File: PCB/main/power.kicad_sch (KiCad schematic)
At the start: 28 parts, among them M1 CJ2301 S1, U1 LP2951-33DR, U2 LM324

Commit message: circuit edits
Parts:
- removed D2: BAT54S, Diode_SMD:D_SOT-23_ANK, symbol Device:D_Schottky
- removed M1: CJ2301 S1, Package_TO_SOT_SMD:SOT-23, symbol pspice:MPMOS
- added D?: ZMM5V1-M, symbol Device:D_Zener
- added Q?: Q_PMOS_SGD, symbol Device:Q_PMOS_SGD
- added Q?: Q_PMOS_GSD, symbol Device:Q_PMOS_GSD
- added R?: 100, symbol Device:R
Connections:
- net +5V (INPUT PROTECTED): now also D?.1 (K), Q?.1 (S)
- net GND: now also R?.2
- net at D6.2 (A): now also Q?.2 (S)
- net at JP3.2 (B), JP4.2 (B): now also Q?.3 (D)
- net at JP6.2 (B), R3.1, U2.4 (V+): now also R5.2, Q?.3 (D); no longer R5.1
- net at D4.1 (K), U2.1 (+): now also R5.1; no longer R5.2
- net at U2.3: now also Q?.1 (G)
- new net: D?.2 (A), Q?.2 (G), R?.1
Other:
- moved on the sheet: D4, D6, JP3, JP4, JP6, R3, R4, R5, R6, U2

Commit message: Small changes
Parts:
- gave numbers to parts that had none: 4
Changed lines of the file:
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@@
   (symbol (lib_id "Device:Q_PMOS_SGD") (at 78.74 90.17 90) (unit 1)
     (in_bom yes) (on_board yes) (fields_autoplaced)
-    (property "Reference" "Q?" (id 0) (at 78.74 80.01 90))
+    (property "Reference" "Q2" (id 0) (at 78.74 80.01 90))
     (property "Value" "Q_PMOS_SGD" (id 1) (at 78.74 82.55 90))
     (property "Footprint" "" (id 2) (at 76.2 85.09 0)
@@
   (symbol (lib_id "Device:D_Zener") (at 88.9 91.44 270) (unit 1)
     (in_bom yes) (on_board yes) (fields_autoplaced)
-    (property "Reference" "D?" (id 0) (at 91.44 90.1699 90)
+    (property "Reference" "D2" (id 0) (at 91.44 90.1699 90)
       (effects (font (size 1.27 1.27)) (justify left))
     )
@@
   (symbol (lib_id "power:GND") (at 78.74 104.14 0) (unit 1)
     (in_bom yes) (on_board yes) (fields_autoplaced)
-    (property "Reference" "#PWR?" (id 0) (at 78.74 110.49 0)
+    (property "Reference" "#PWR019" (id 0) (at 78.74 110.49 0)
       (effects (font (size 1.27 1.27)) hide)
     )
@@
   (symbol (lib_id "Device:Q_PMOS_GSD") (at 255.27 50.8 0) (unit 1)
     (in_bom yes) (on_board yes) (fields_autoplaced)
-    (property "Reference" "Q?" (id 0) (at 261.62 49.5299 0)
+    (property "Reference" "Q3" (id 0) (at 261.62 49.5299 0)
       (effects (font (size 1.27 1.27)) (justify left))
     )
@@
   (symbol (lib_id "Device:R") (at 78.74 100.33 0) (unit 1)
     (in_bom yes) (on_board yes) (fields_autoplaced)
-    (property "Reference" "R?" (id 0) (at 81.28 99.0599 0)
-      (effects (font (size 1.27 1.27)) (justify left))
-    )
+    (property "Reference" "R19" (id 0) (at 81.28 99.0599 0)
+      (effects (font (size 1.27 1.27)) (justify left))
+    )

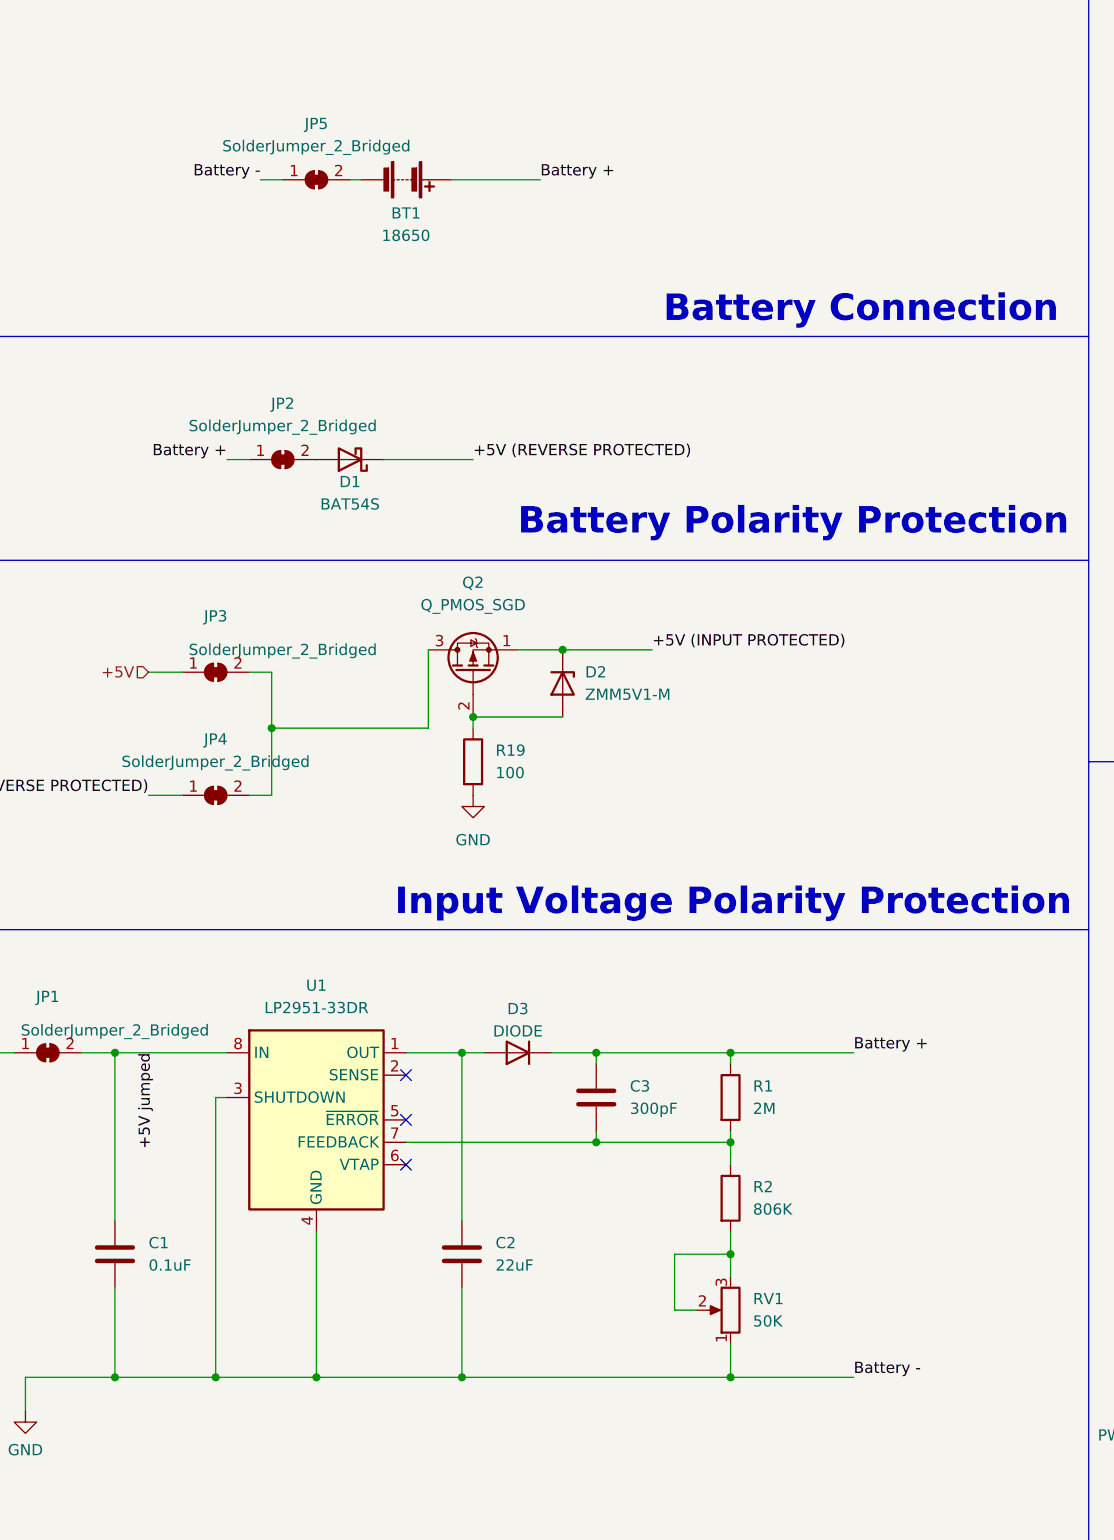
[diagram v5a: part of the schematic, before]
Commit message: Change labels
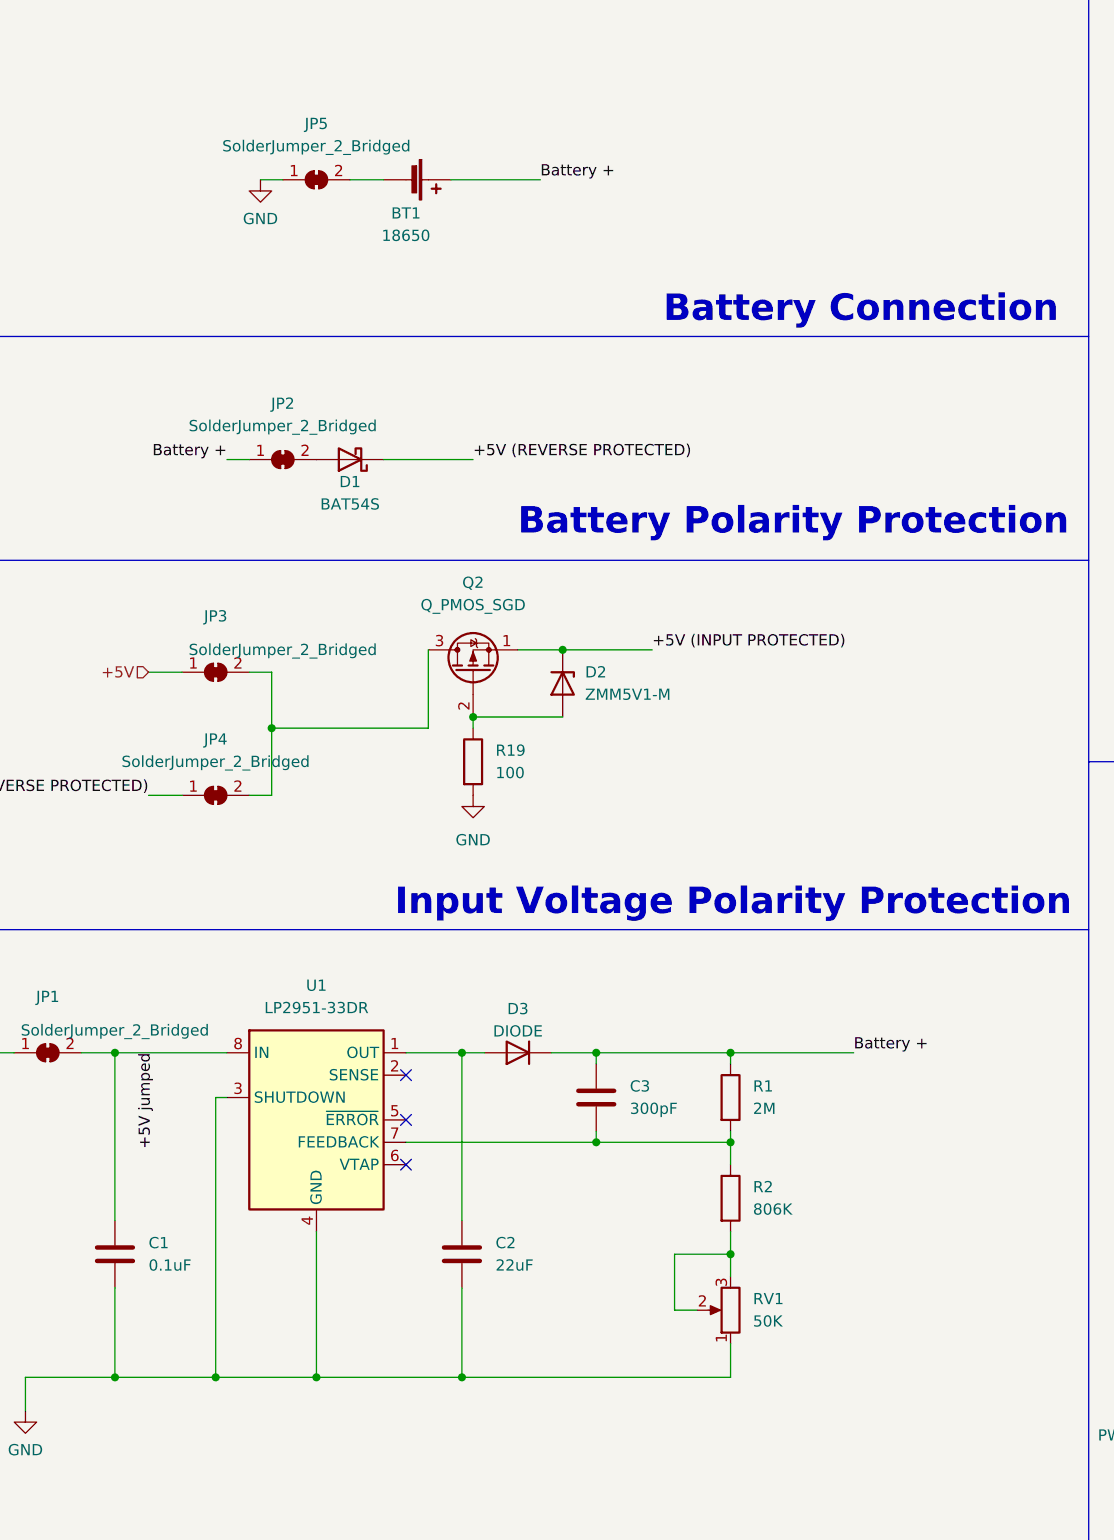
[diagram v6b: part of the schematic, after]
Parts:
- BT1: symbol Device:Battery -> Device:Battery_Cell
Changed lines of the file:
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@@
   (junction (at 78.74 95.25) (diameter 0) (color 0 0 0 0)
-  )
-  (junction (at 107.95 170.18) (diameter 0) (color 0 0 0 0)
   )
   (junction (at 55.88 96.52) (diameter 0) (color 0 0 0 0)
@@
     (stroke (width 0) (type default) (color 0 0 0 0))
   )
-  (wire (pts (xy 107.95 170.18) (xy 121.92 170.18))
-    (stroke (width 0) (type default) (color 0 0 0 0))
-  )
   (wire (pts (xy 71.12 133.35) (xy 77.47 133.35))
     (stroke (width 0) (type default) (color 0 0 0 0))
@@
     (stroke (width 0) (type default) (color 0 0 0 0))
   )
-  (wire (pts (xy 64.77 34.29) (xy 66.04 34.29))
+  (wire (pts (xy 64.77 34.29) (xy 68.58 34.29))
     (stroke (width 0) (type default) (color 0 0 0 0))
   )
@@
   (label "Battery +" (at 166.37 31.75 180)
     (effects (font (size 1.27 1.27)) (justify right bottom))
-  )
-  (label "Battery -" (at 54.61 34.29 180)
-    (effects (font (size 1.27 1.27)) (justify right bottom))
-  )
-  (label "Battery -" (at 121.92 170.18 0)
-    (effects (font (size 1.27 1.27)) (justify left bottom))
   )
   (label "+5V (INPUT PROTECTED)" (at 99.06 87.63 0)
@@
     (pin "2")
   )
-  (symbol (lib_id "Device:Battery") (at 71.12 34.29 270) (unit 1)
+  (symbol (lib_id "Device:Battery_Cell") (at 71.12 34.29 270) (unit 1)
     (in_bom yes) (on_board yes)
     (property "Reference" "BT1" (id 0) (at 71.12 38.1 90))
@@
     (pin "3")
   )
+  (symbol (lib_id "power:GND") (at 54.61 34.29 0) (unit 1)
+    (in_bom yes) (on_board yes) (fields_autoplaced)
+    (property "Reference" "#PWR?" (id 0) (at 54.61 40.64 0)
+      (effects (font (size 1.27 1.27)) hide)
+    )
+    (property "Value" "GND" (id 1) (at 54.61 38.7334 0))
+    (property "Footprint" "" (id 2) (at 54.61 34.29 0)
+      (effects (font (size 1.27 1.27)) hide)
+    )
+    (property "Datasheet" "" (id 3) (at 54.61 34.29 0)
+      (effects (font (size 1.27 1.27)) hide)
+    )
+    (pin "1")
+  )
   (symbol (lib_id "Simulation_SPICE:DIODE") (at 83.82 133.35 0) (unit 1)

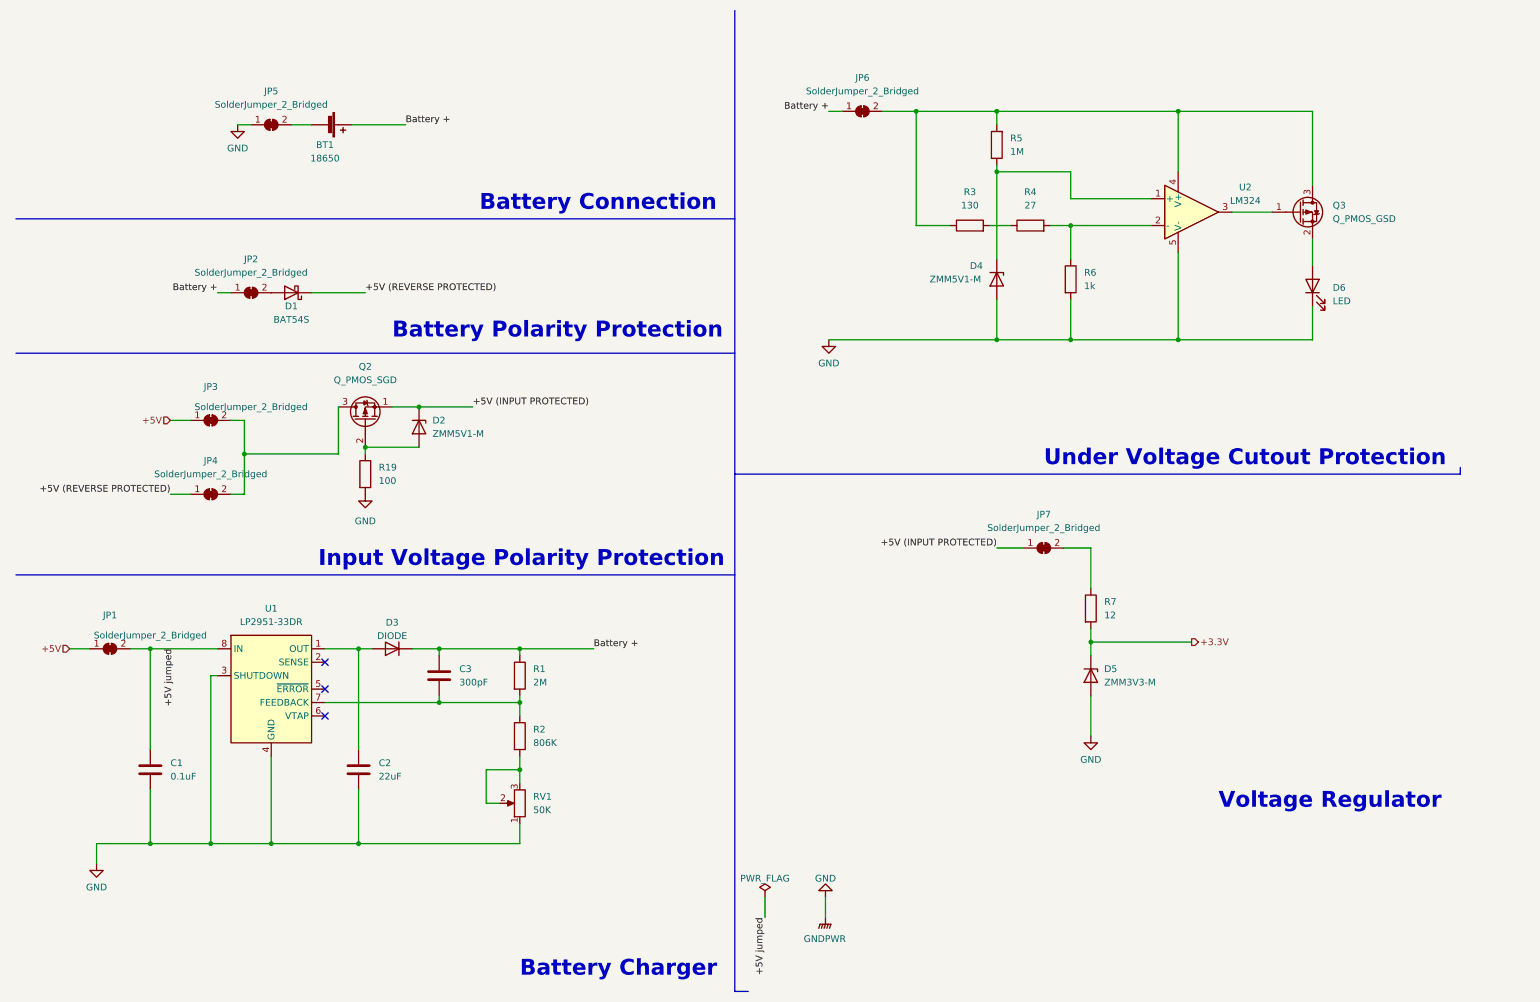
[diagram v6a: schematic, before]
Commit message: Add voltage regulator
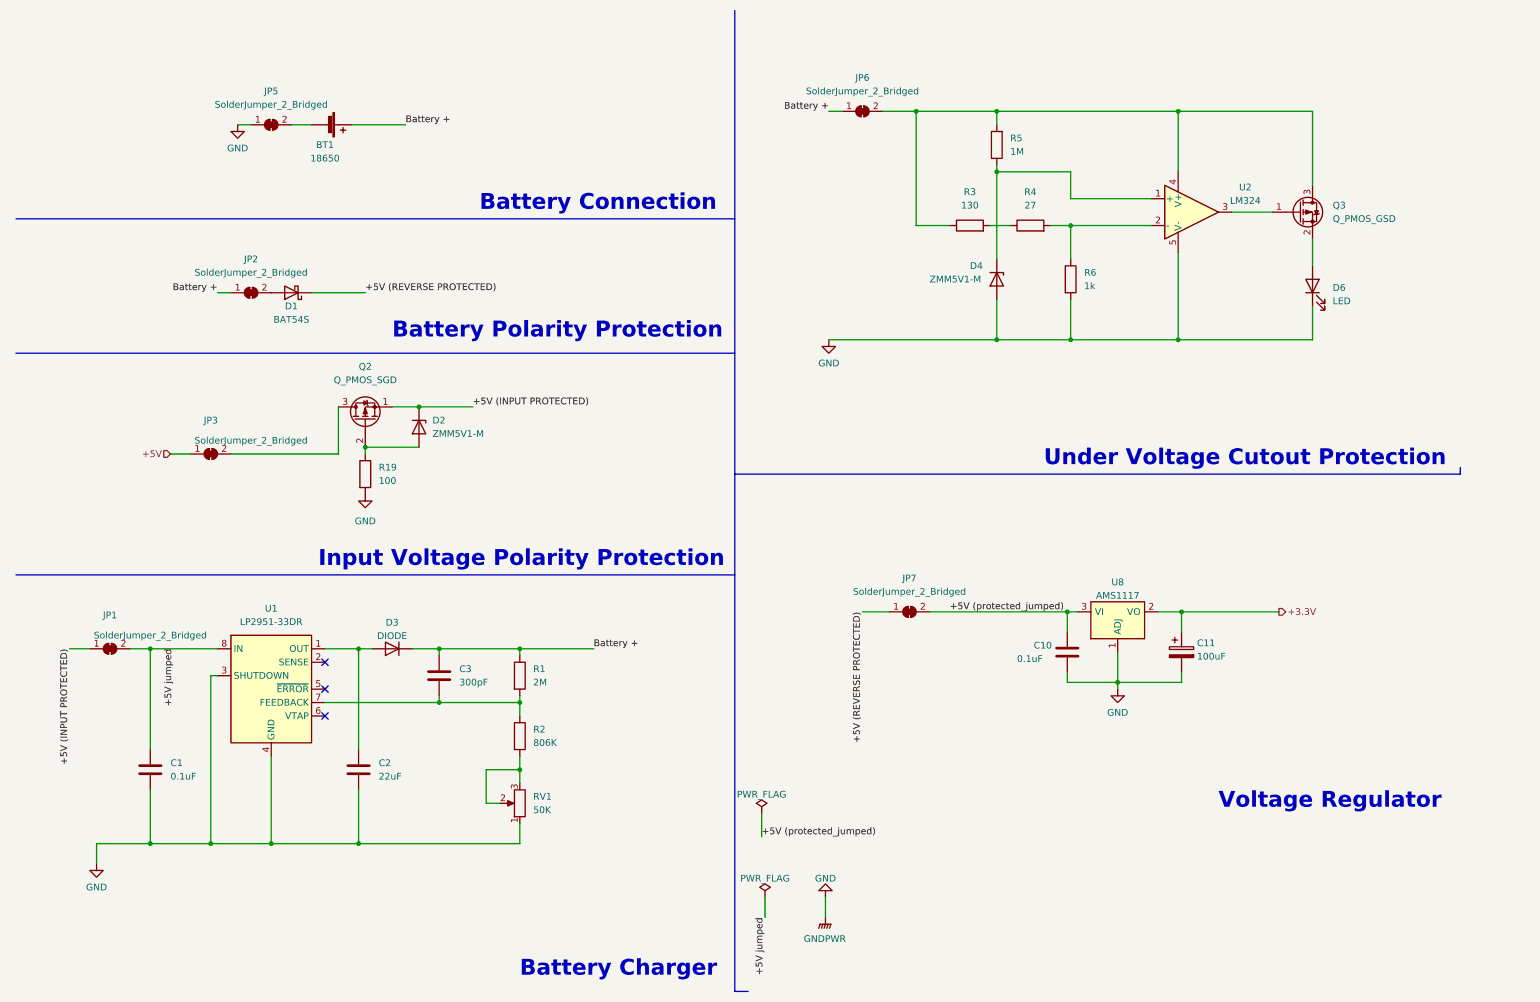
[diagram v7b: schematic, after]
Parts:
- removed D5: ZMM3V3-M, Footprint_EEE3088F:LL-34_L3.5-W1.5-RD, symbol Device:D_Zener
- removed JP4: SolderJumper_2_Bridged, Jumper:SolderJumper-2_P1.3mm_Bridged2Bar_Pad1.0x1.5mm, symbol Jumper:SolderJumper_2_Bridged
- removed R7: 12, Resistor_SMD:R_1206_3216Metric, symbol Device:R
- added C10: 0.1uF, Capacitor_SMD:C_0402_1005Metric, symbol Device:C
- added C11: 100uF, symbol Device:C_Polarized
- added U8: AMS1117, Package_TO_SOT_SMD:SOT-223-3_TabPin2, symbol Regulator_Linear:AMS1117
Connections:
- net +3.3V: now also C11.1, U8.2 (VO)
- net +5V: no longer JP1.1 (A)
- net +5V (INPUT PROTECTED): now also JP1.1 (A); no longer JP7.1 (A)
- net +5V (REVERSE PROTECTED): now also JP7.1 (A)
- net GND: now also C10.2, C11.2, U8.1 (ADJ)
- net +5V (protected_jumped): now reaches JP7.2 (B)
- net +5V (protected_jumped): now also C10.1, U8.3 (VI)
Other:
- moved on the sheet: JP3, JP7

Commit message: add hierachal sheet
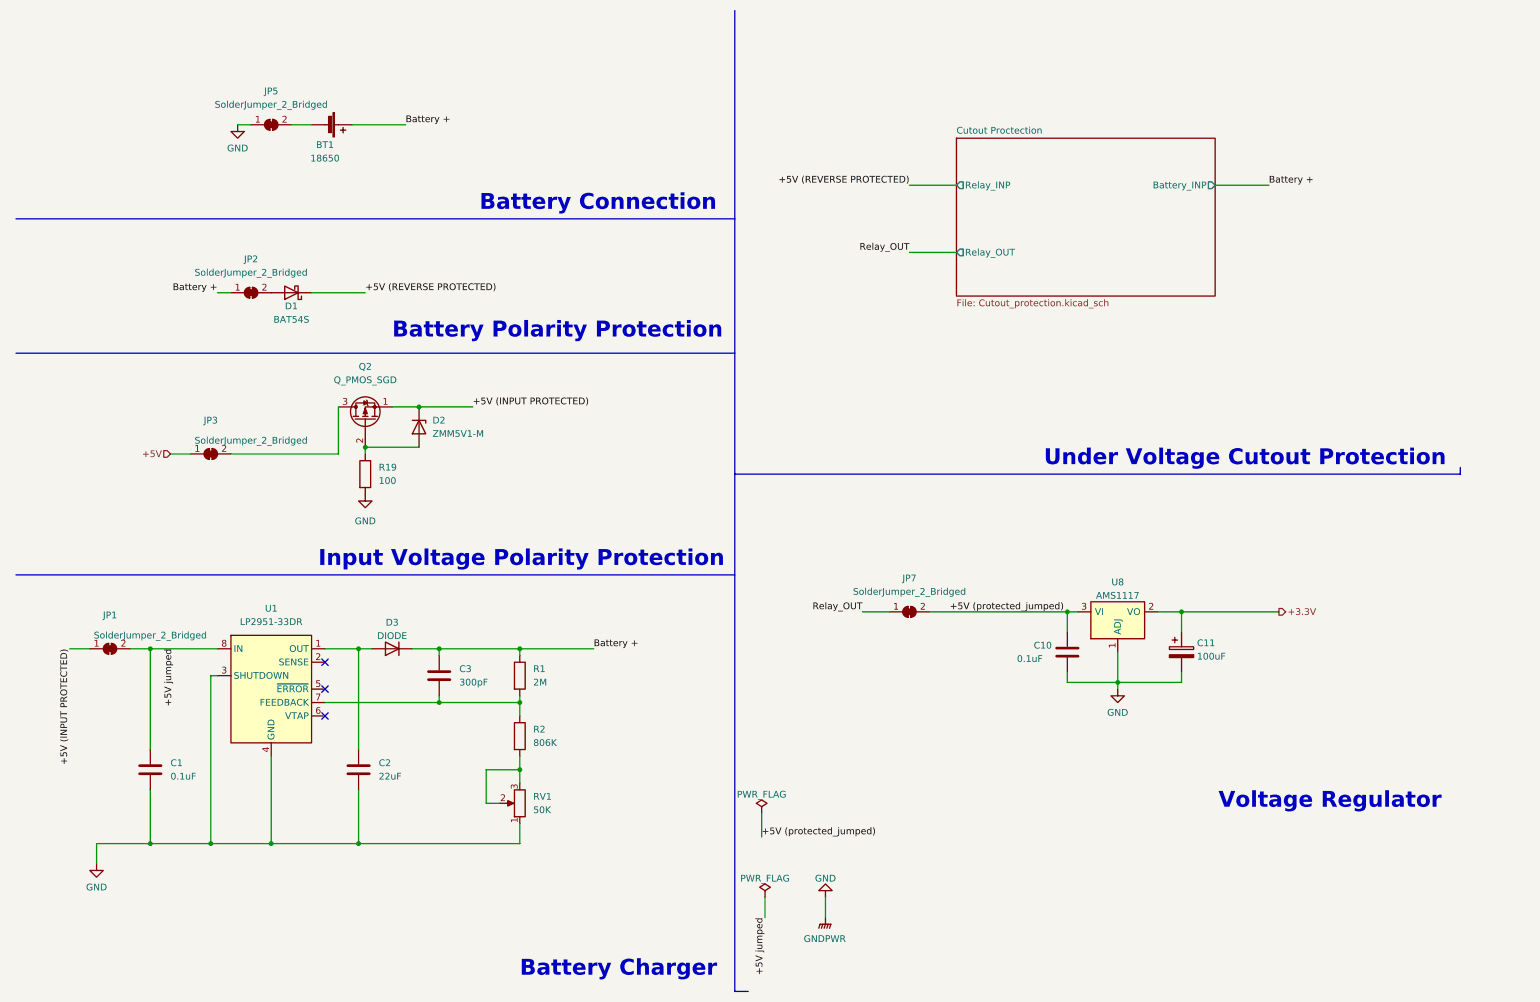
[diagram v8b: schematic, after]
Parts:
- removed D4: ZMM5V1-M, Footprint_EEE3088F:LL-34_L3.5-W1.5-RD, symbol Device:D_Zener
- removed D6: LED, LED_SMD:LED_0603_1608Metric, symbol Device:LED
- removed JP6: SolderJumper_2_Bridged, Jumper:SolderJumper-2_P1.3mm_Bridged2Bar_Pad1.0x1.5mm, symbol Jumper:SolderJumper_2_Bridged
- removed Q3: Q_PMOS_GSD, symbol Device:Q_PMOS_GSD
- removed R3: 130, Resistor_SMD:R_0402_1005Metric, symbol Device:R
- removed R4: 27, Resistor_SMD:R_0603_1608Metric, symbol Device:R
- removed R5: 1M, Resistor_SMD:R_0402_1005Metric, symbol Device:R
- removed R6: 1k, Resistor_SMD:R_0402_1005Metric, symbol Device:R
- removed U2: LM324, symbol pspice:OPAMP
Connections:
- net +5V (REVERSE PROTECTED): no longer JP7.1 (A)
- new net Relay_OUT: JP7.1 (A)
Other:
- added sheet Cutout Proctection (Cutout_protection.kicad_sch)
